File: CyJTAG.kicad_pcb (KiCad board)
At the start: 2 copper layers, 33.7 x 21.6 mm, 9 parts, among them P1 USB_B, P2 CONN_01X10, P3 CONN_01X06, P4 CONN_01X06, U1 CY7C65215

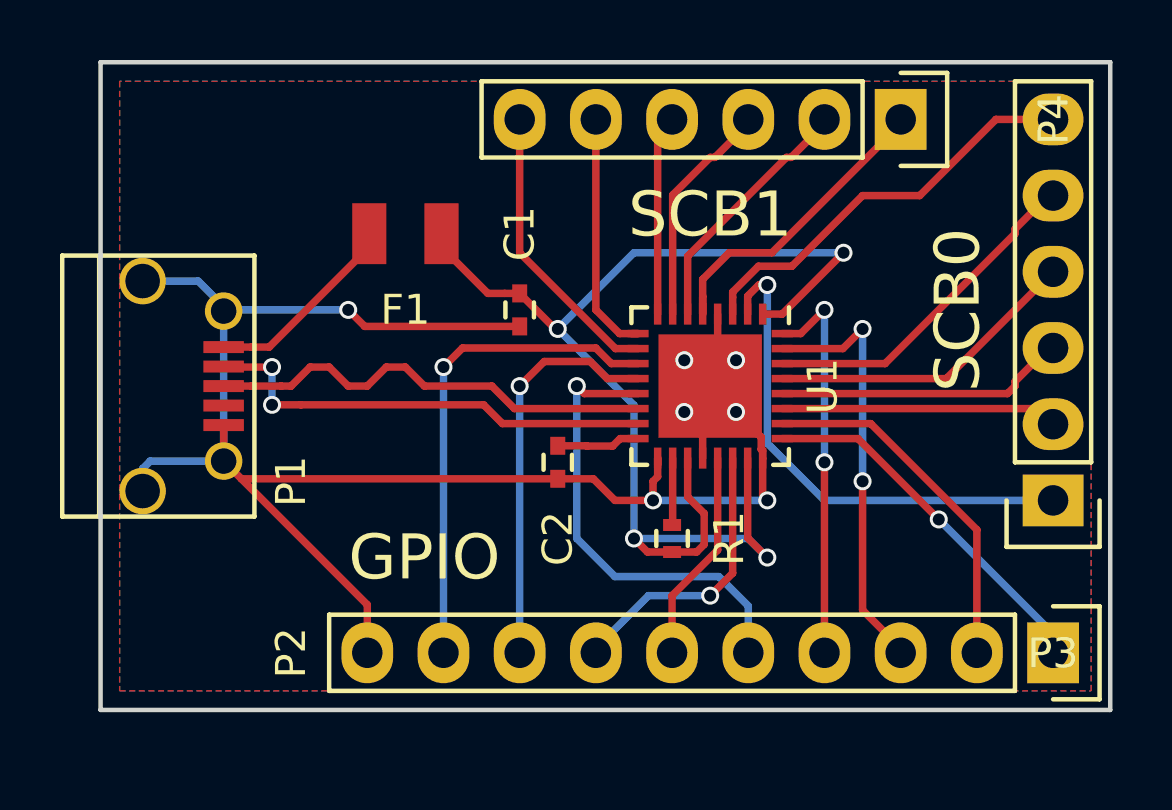
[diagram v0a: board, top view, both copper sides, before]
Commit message: Updated board to switch between 5V and 3.3V
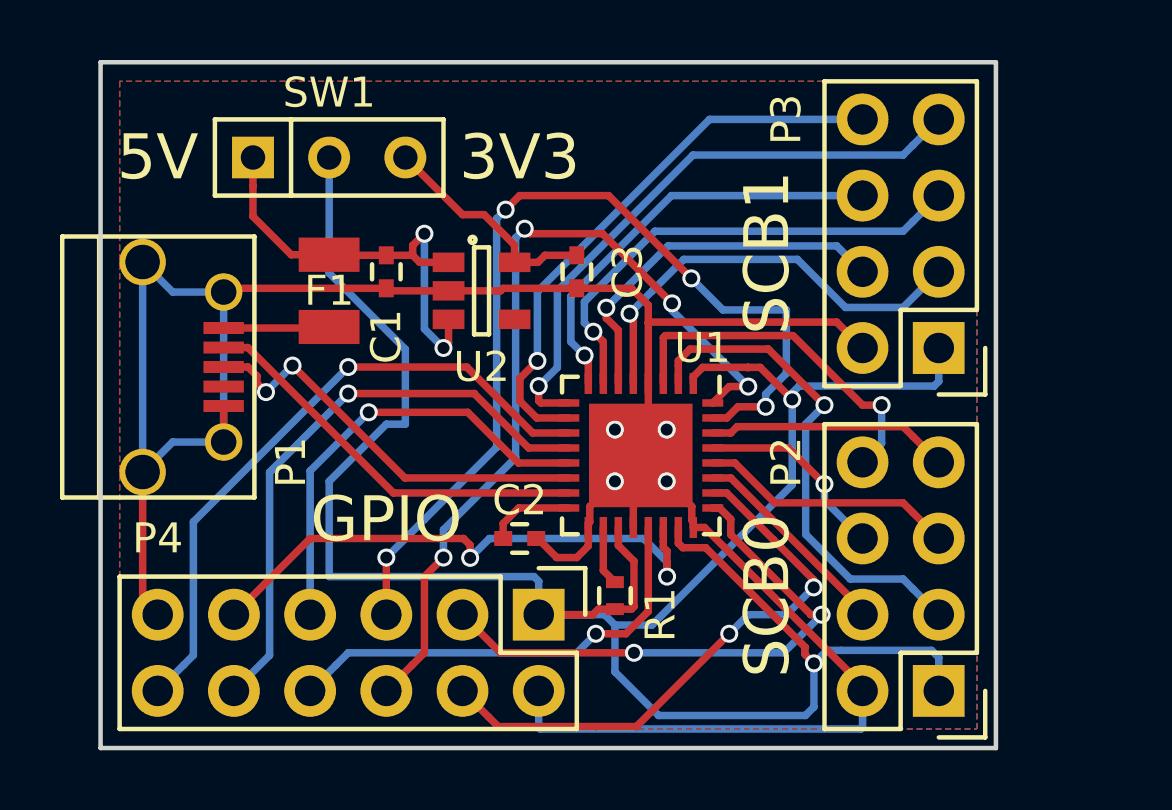
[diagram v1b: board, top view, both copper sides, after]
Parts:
- added ?: Symbol_OSHW-Logo_SilkScreen, Symbols:Symbol_OSHW-Logo_SilkScreen, B.Cu at (119.4, 109.7)
- added C3: 1.0uF, Capacitors_SMD:C_0402, F.Cu at (113.7, 101.6)
- added SW1: Switch_SPDT, Buttons_Switches_ThroughHole:SW_Micro_SPST, F.Cu at (105.4, 97.8)
- added U2: TLV70233DBV, TO_SOT_Packages_SMD:SOT-23-5, F.Cu at (110.5, 102.2)
- P2: value CONN_01X10 -> CONN_02X04; footprint Pin_Headers:Pin_Header_Straight_1x10 -> Pin_Headers:Pin_Header_Straight_2x04
- P3: value CONN_01X06 -> CONN_02X04; footprint Pin_Headers:Pin_Header_Straight_1x06 -> Pin_Headers:Pin_Header_Straight_2x04
- P4: value CONN_01X06 -> CONN_02X06; footprint Pin_Headers:Pin_Header_Straight_1x06 -> Pin_Headers:Pin_Header_Straight_2x06
- moved P4 20.4 mm to (112.4, 113.0)
- moved P3 6.35 mm to (125.7, 104.1)
- moved C1 4.62 mm to (107.3, 101.6)
- moved P2 4.02 mm to (125.7, 115.6), turned to 180 degrees
- moved U1 3.27 mm to (115.8, 107.7)
- moved F1 3.18 mm to (105.4, 102.2), turned to 90 degrees
- moved C2 2.84 mm to (111.8, 110.5), turned to 0 degrees
- moved R1 2.69 mm to (114.9, 112.4)
- moved P1 0.63 mm to (100.3, 104.8)
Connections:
- net Net-(P1-Pad2) renamed /USBDP
- net Net-(P1-Pad3) renamed /USBDM
- C1 pad 1: VDD -> +5V
- F1 pad 1: VDD -> Net-(F1-Pad1)
- F1 pad 2: Net-(F1-Pad2) -> +5V
- P1 pad 1: Net-(F1-Pad2) -> Net-(F1-Pad1)
- P2 pad 1: /GPIO_0 -> VDD
- P2 pad 2: /GPIO_1 -> GND
- P2 pad 3: /GPIO_6 -> /SCB0_0
- P2 pad 4: /GPIO_7 -> /SCB0_1
- P2 pad 5: /GPIO_16 -> /SCB0_2
- P2 pad 6: /GPIO_17 -> /SCB0_3
- P2 pad 7: /GPIO_18 -> /SCB0_4
- P2 pad 8: /WAKEUP -> /SCB0_5
- P3 pad 1: Net-(P3-Pad1) -> VDD
- P3 pad 2: Net-(P3-Pad2) -> GND
- P3 pad 3: Net-(P3-Pad3) -> /SCB1_0
- P3 pad 4: Net-(P3-Pad4) -> /SCB1_1
- P3 pad 5: Net-(P3-Pad5) -> /SCB1_2
- P3 pad 6: Net-(P3-Pad6) -> /SCB1_3
- P4 pad 1: Net-(P4-Pad1) -> VDD
- P4 pad 2: Net-(P4-Pad2) -> GND
- P4 pad 3: Net-(P4-Pad3) -> /GPIO_0
- P4 pad 4: Net-(P4-Pad4) -> /GPIO_1
- P4 pad 5: Net-(P4-Pad5) -> /GPIO_6
- P4 pad 6: Net-(P4-Pad6) -> /GPIO_7
- U1 pad 10: Net-(P4-Pad6) -> /SCB1_5
- U1 pad 2: Net-(P3-Pad1) -> /SCB0_0
- U1 pad 27: Net-(P3-Pad2) -> /SCB0_1
- U1 pad 28: Net-(P3-Pad3) -> /SCB0_2
- U1 pad 29: Net-(P3-Pad4) -> /SCB0_3
- U1 pad 3: Net-(P3-Pad6) -> /SCB0_5
- U1 pad 30: Net-(P3-Pad5) -> /SCB0_4
- U1 pad 5: Net-(P4-Pad1) -> /SCB1_0
- U1 pad 6: Net-(P4-Pad2) -> /SCB1_1
- U1 pad 7: Net-(P4-Pad3) -> /SCB1_2
- U1 pad 8: Net-(P4-Pad4) -> /SCB1_3
- U1 pad 9: Net-(P4-Pad5) -> /SCB1_4
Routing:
- net VDD: track 41.6 -> 77.4 mm, vias 4 -> 2
- net GND: track 64.8 -> 87.4 mm, vias 7 -> 4
- net /SCB1_4: track 0.00 -> 20.0 mm, vias 0 -> 1
- net /SCB1_5: track 0.00 -> 19.0 mm, vias 0 -> 1
- net /GPIO_6: track 14.3 -> 31.7 mm, vias 2 -> 4
- net Net-(P3-Pad1): track 17.0 -> 0.00 mm, vias 1 -> 0
- net /SCB0_0: track 0.00 -> 16.7 mm, vias 0 -> 1
- net /SCB1_2: track 0.00 -> 16.3 mm, vias 0 -> 1
- net /GPIO_7: track 13.2 -> 28.5 mm, vias 2 -> 4
- net +5V: track 0.00 -> 15.1 mm, vias 0 -> 2
- net /SCB1_0: track 0.00 -> 14.6 mm, vias 0 -> 1
- net /SCB1_3: track 0.00 -> 14.3 mm, vias 0 -> 1
- net Net-(P3-Pad6): track 13.8 -> 0.00 mm
- net /SCB1_1: track 0.00 -> 12.4 mm, vias 0 -> 1
- net /SCB0_5: track 0.00 -> 12.0 mm, vias 0 -> 1
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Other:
- board size 33.7 x 21.6 mm -> 29.8 x 22.9 mm
- board text added: "3V3"
- board text added: "5V"
- board text added: "CC-BY-SA 4.0"
- board text added: "CyJTAGSPI2C"
- board text added: "©2015 Forest Crossman"
- board text removed: "CY7C65215 Breakout Board"

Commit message: Removed unnecessary resistor and corrected VBUS source
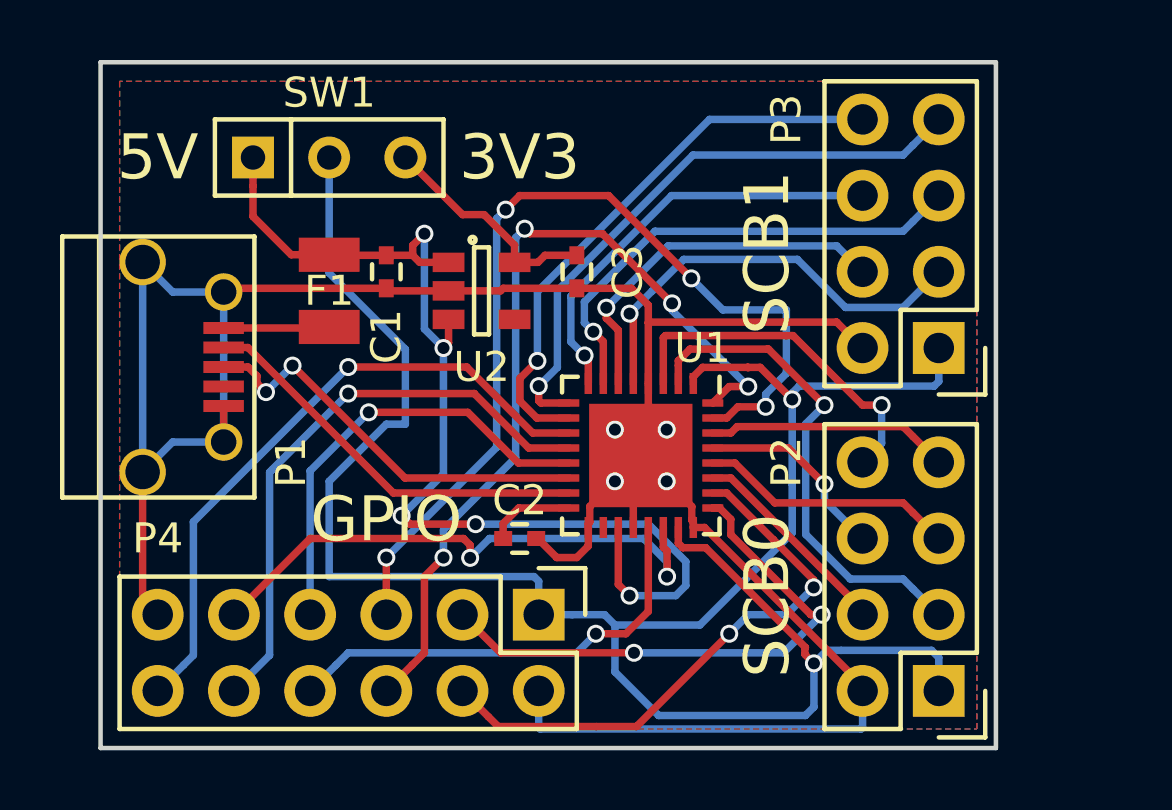
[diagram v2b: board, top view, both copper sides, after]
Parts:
- removed R1: 4.7k, Resistors_SMD:R_0402
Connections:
- U1 pad 18: Net-(R1-Pad2) -> (no net)
- U1 pad 19: VDD -> +5V
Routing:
- net +5V: track 15.1 -> 36.6 mm, vias 2 -> 5
- net VDD: track 77.4 -> 72.2 mm
- net Net-(R1-Pad2): track 1.98 -> 0.00 mm

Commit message: Moved the voltage switch, some of the silkscreen text, and optimized some paths
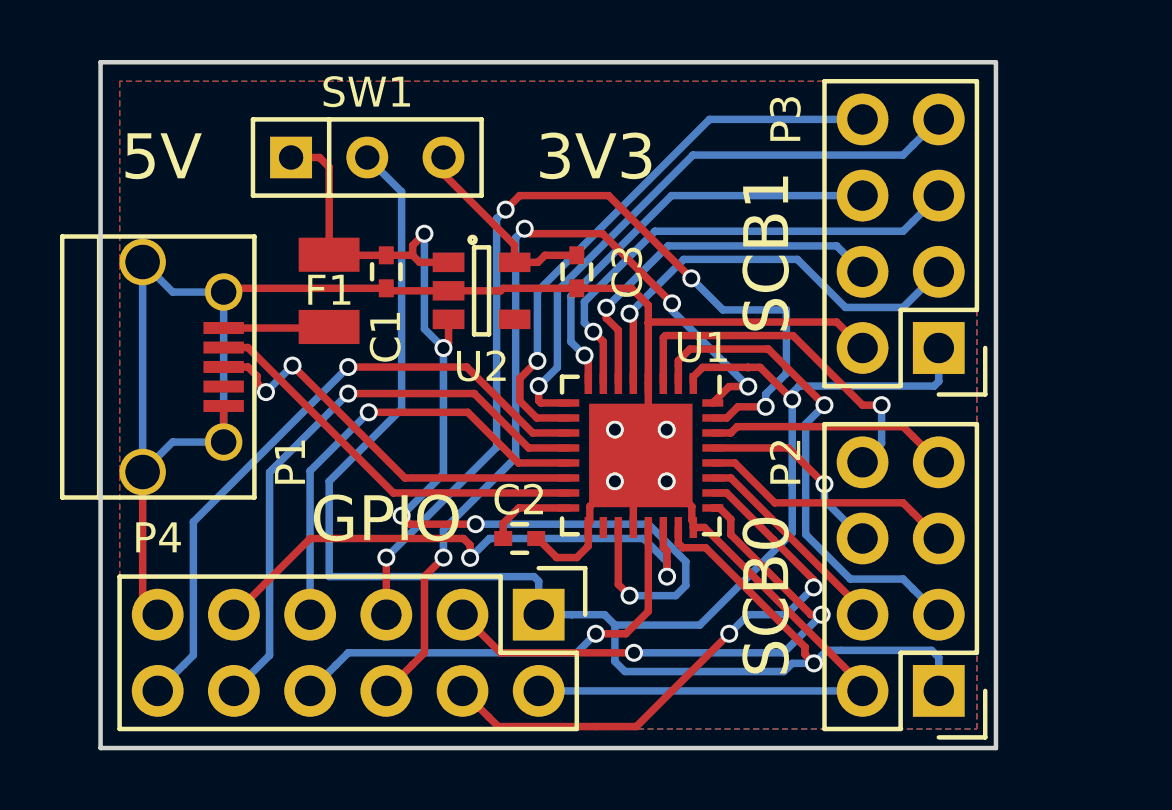
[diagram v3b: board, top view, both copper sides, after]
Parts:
- moved ? 1.61 mm to (117.9, 109.2)
- moved SW1 1.27 mm to (106.7, 97.8)
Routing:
- net VDD: track 72.2 -> 68.9 mm
- net GND: track 87.4 -> 84.9 mm
- net +3V3: track 7.60 -> 6.65 mm
- net +5V: track 36.6 -> 35.9 mm
